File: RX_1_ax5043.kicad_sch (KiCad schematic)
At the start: 18 parts, among them U201 RFShield_OnePiece, U205 AX5043, U206 TPS22919D

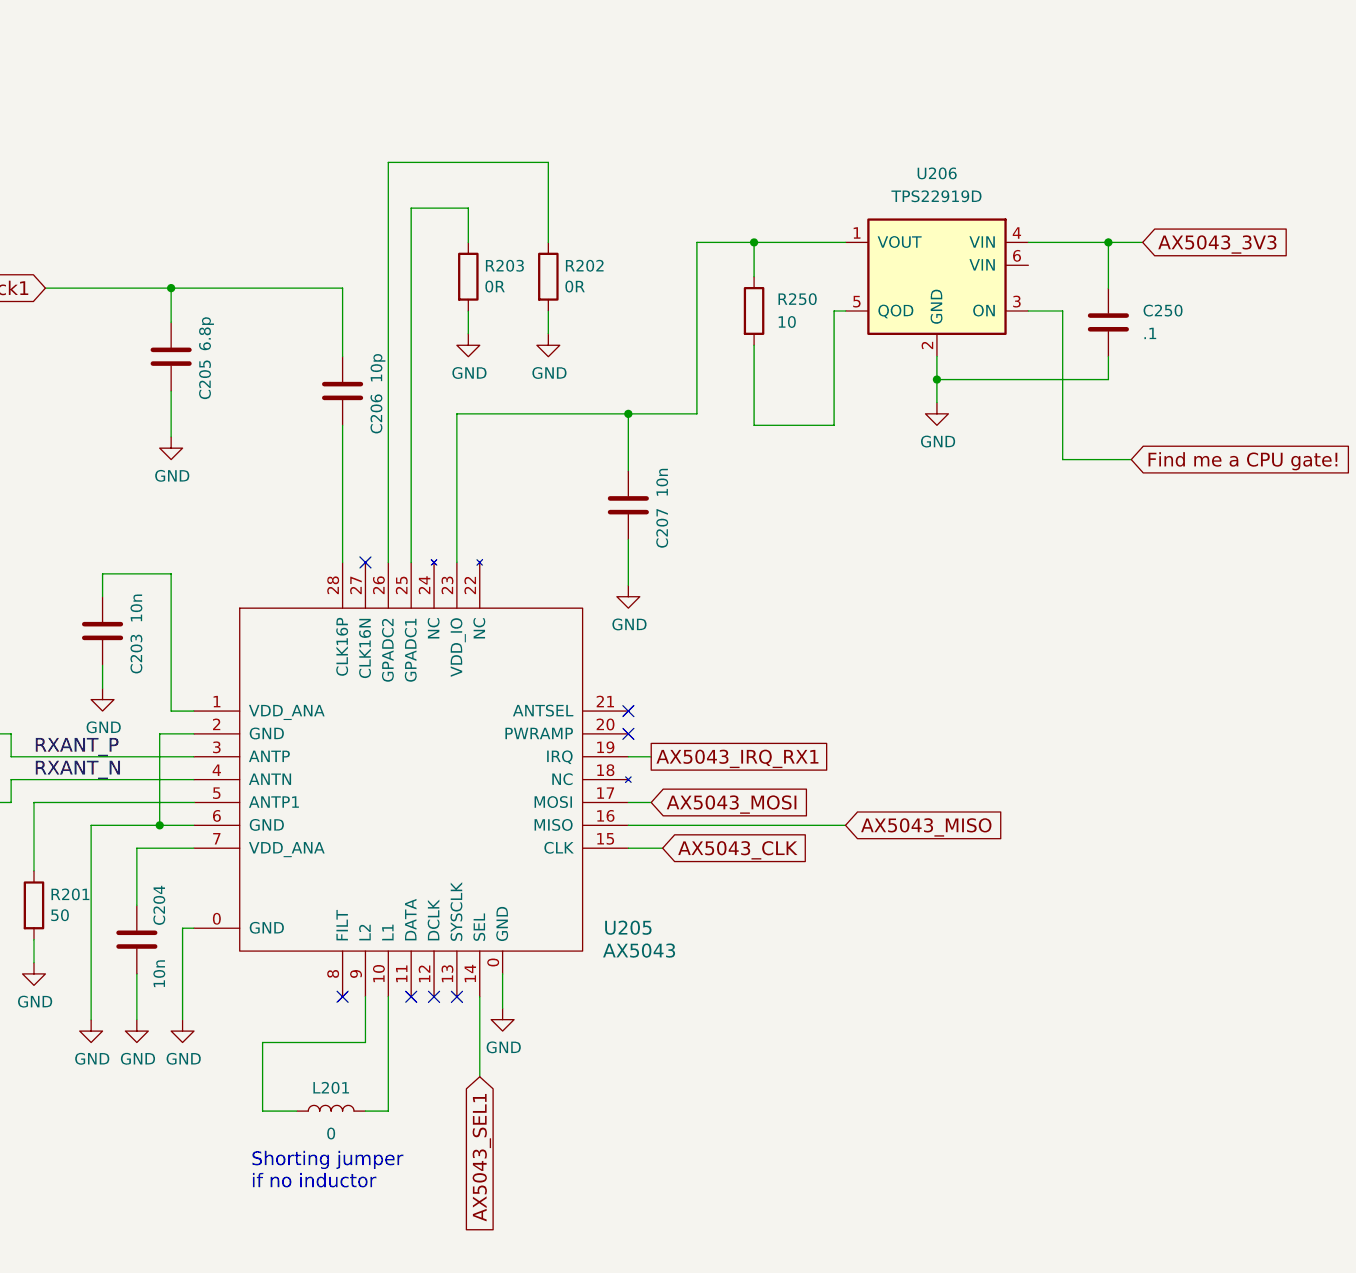
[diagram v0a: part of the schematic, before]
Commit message: Lots of cleanups to fix numerous issues
Signed-off-by: Corey Minyard <corey@minyard.net>
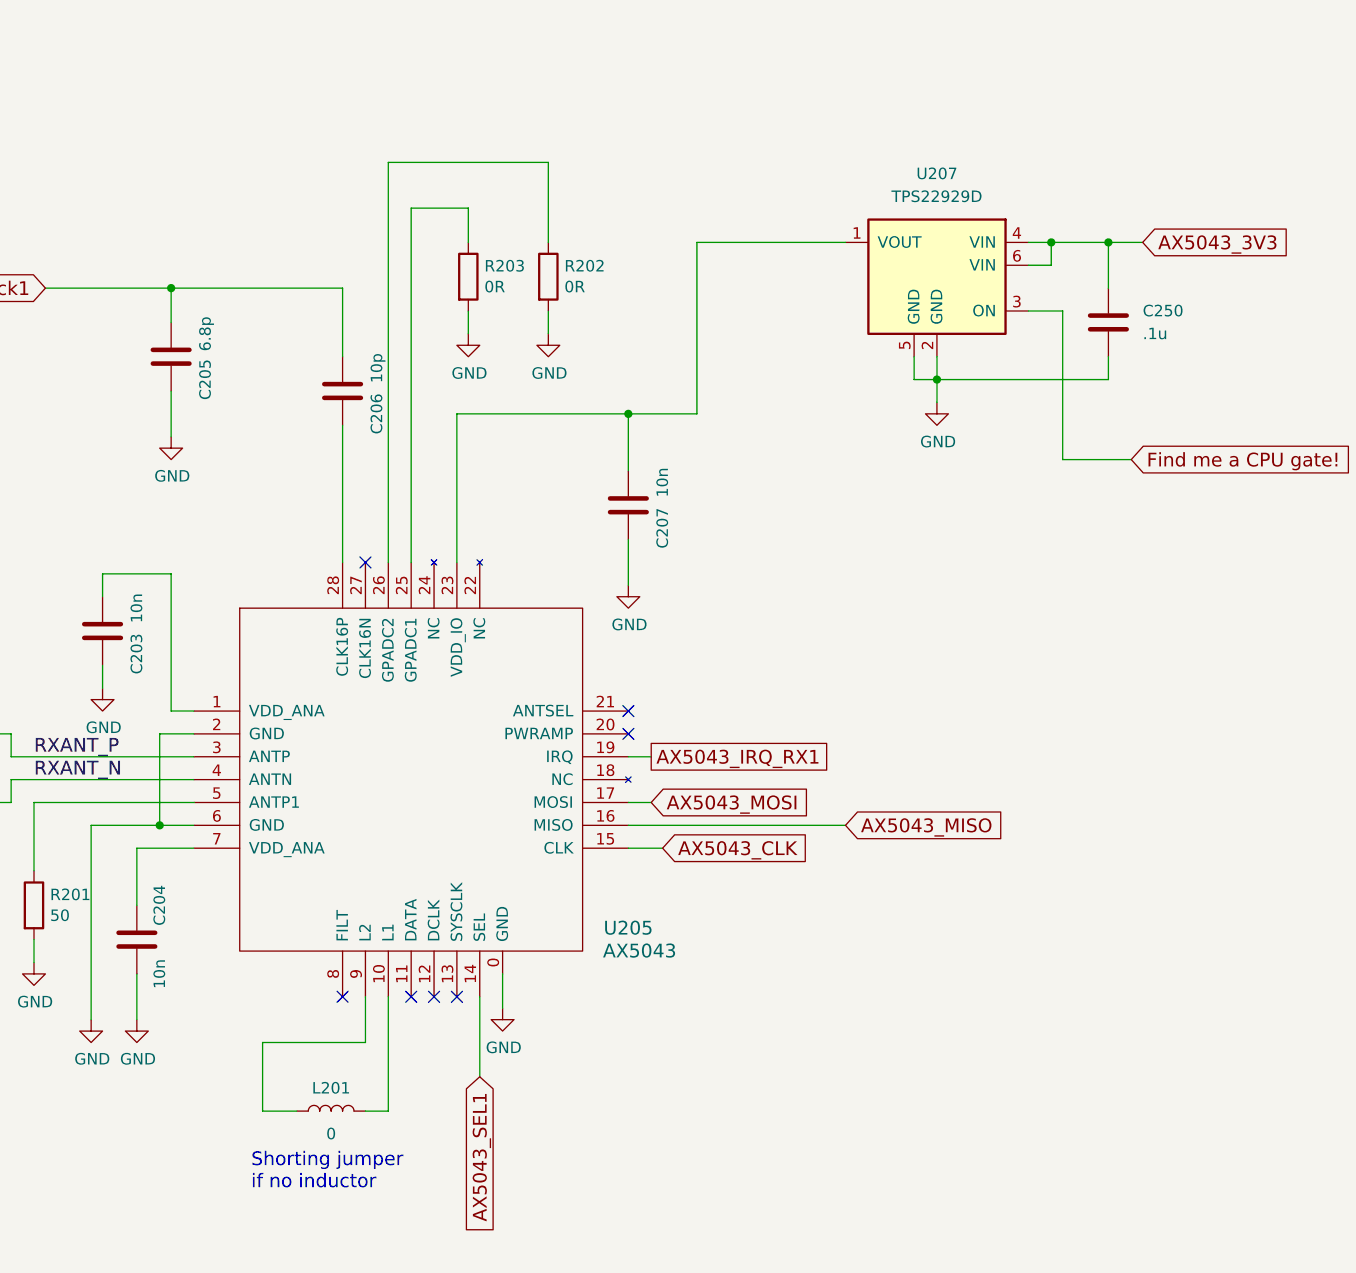
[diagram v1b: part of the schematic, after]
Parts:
- removed R250: 10, symbol Device:R
- C250: value .1 -> .1u; footprint (none) -> Capacitor_SMD:C_0402_1005Metric
- U207: renamed from U206; value TPS22919D -> TPS22929D
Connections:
- net AX5043_3V3: now also U207.6 (VIN)
- net GND: now also U207.5 (GND)

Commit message: Start ripping things apart
Signed-off-by: Corey Minyard <corey@minyard.net>
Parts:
- removed C201, C202: 4p3, Capacitor_SMD:C_0603_1608Metric_Pad1.08x0.95mm_HandSolder, symbol Device:C
- removed P202: ~, PacSatDev_misc:U_FL, symbol PACSAT_DEV_misc:U_FL
- added L90: WBC1-1TL, IND6_WBC1, symbol PACSAT_DEV_misc:WBC1-1TL
- added R89: 10K, Resistor_SMD:R_0603_1608Metric_Pad0.98x0.95mm_HandSolder, symbol Device:R
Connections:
- net GND: now also L90.2, L90.4, R89.2
- net RXANT_N: now also L90.3
- net RXANT_P: now also L90.1
- net Find me a CPU gate! renamed AX5043_EN_RX1
- net AX5043_EN_RX1: now also R89.1
- net RX1_P: no longer names the net of P201.1 (In)
- net RX1_P: now also L90.6
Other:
- note removed: "RX1-"
- note removed: "Short Caps Initially"
- moved on the sheet: P201

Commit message: More hacking on things
Signed-off-by: Corey Minyard <corey@minyard.net>
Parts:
- removed U201: RFShield_OnePiece, PacSatDev_misc:RF_SHIELD_BMI_S_201_F_U201, symbol PACSAT_DEV_misc:RF_SHIELD_BOX

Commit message: Clean up RTC, start working on power
Signed-off-by: Corey Minyard <corey@minyard.net>
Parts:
- L90: footprint IND6_WBC1 -> PacSatDev_misc:IND6_WBC1
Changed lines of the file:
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@@
 			)
 		)
-		(property "Footprint" "IND6_WBC1"
+		(property "Footprint" "PacSatDev_misc:IND6_WBC1"
 			(at 170.18 129.54 0)
 			(effects

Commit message: Finish up most of the ax5043 routing
Signed-off-by: Corey Minyard <corey@minyard.net>
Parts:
- L201: footprint PacSatDev_misc:L_Murata_LQH2MCNxxxx02_2.0x1.6mm -> Inductor_SMD:L_0603_1608Metric_Pad1.05x0.95mm_HandSolder
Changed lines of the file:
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@@
 			)
 		)
-		(property "Footprint" "PacSatDev_misc:L_Murata_LQH2MCNxxxx02_2.0x1.6mm"
+		(property "Footprint" "Inductor_SMD:L_0603_1608Metric_Pad1.05x0.95mm_HandSolder"
 			(at 212.09 172.72 0)
 			(effects

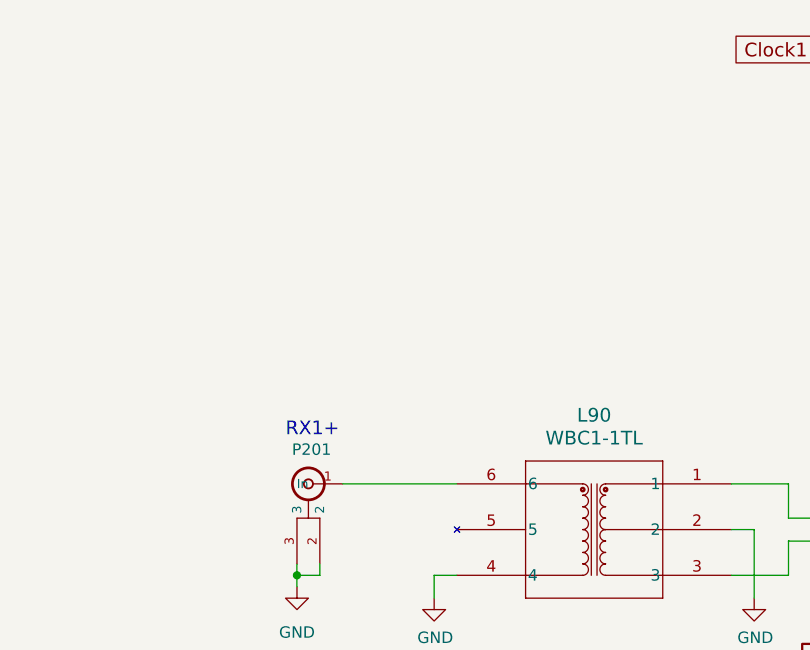
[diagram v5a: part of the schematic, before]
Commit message: Do a lot of routing work
RX input is done, 5043s are done, power is done.

Signed-off-by: Corey Minyard <corey@minyard.net>
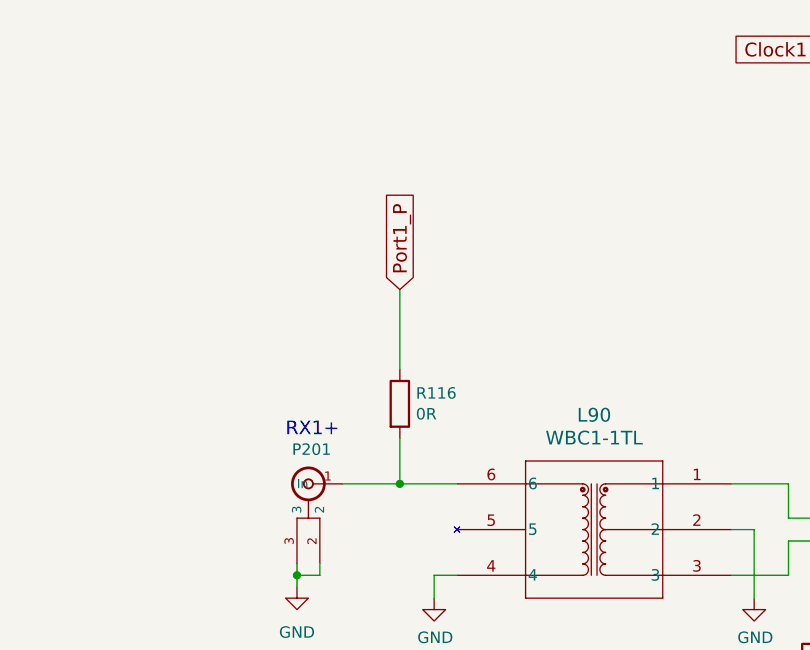
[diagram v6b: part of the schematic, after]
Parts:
- added R116: 0R, Resistor_SMD:R_0603_1608Metric_Pad0.98x0.95mm_HandSolder, symbol Device:R
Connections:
- net at L90.6, P201.1 (In): now also R116.2
- new net Port1_P: R116.1
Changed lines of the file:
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@@
+	)
+	(junction
+		(at 133.35 129.54)
+		(diameter 0)
+		(color 0 0 0 0)
 	)
 	(junction
@@
 	(wire
 		(pts
+			(xy 133.35 129.54) (xy 139.7 129.54)
+		)
+		(stroke
+			(width 0)
+			(type default)
+		)
+	)
+	(wire
+		(pts
 			(xy 279.4 91.44) (xy 298.45 91.44)
 		)
@@
 	(wire
 		(pts
-			(xy 127 129.54) (xy 139.7 129.54)
+			(xy 127 129.54) (xy 133.35 129.54)
 		)
 		(stroke
@@
 	(wire
 		(pts
+			(xy 133.35 124.46) (xy 133.35 129.54)
+		)
+		(stroke
+			(width 0)
+			(type default)
+		)
+	)
+	(wire
+		(pts
 			(xy 245.11 138.43) (xy 247.65 138.43)
 		)
@@
 		(pts
 			(xy 196.85 143.51) (xy 190.5 143.51)
+		)
+		(stroke
+			(width 0)
+			(type default)
+		)
+	)
+	(wire
+		(pts
+			(xy 133.35 107.95) (xy 133.35 116.84)
 		)
 		(stroke
@@
 		(property "Intersheetrefs" "${INTERSHEET_REFS}"
 			(at 265.6275 143.51 0)
+			(effects
+				(font
+					(size 1.27 1.27)
+				)
+				(justify left)
+				(hide yes)
+			)
+		)
+	)
+	(global_label "Port1_P"
+		(shape input)
+		(at 133.35 107.95 90)
+		(fields_autoplaced yes)
+		(effects
+			(font
+				(size 1.524 1.524)
+			)
+			(justify left)
+		)
+		(property "Intersheetrefs" "${INTERSHEET_REFS}"
+			(at 133.35 96.2995 90)
 			(effects
 				(font
@@
 					(unit 1)
 				)
+			)
+		)
+	)
+	(symbol
+		(lib_id "Device:R")
+		(at 133.35 120.65 0)
+		(unit 1)
+		(exclude_from_sim no)
+		(in_bom yes)
+		(on_board yes)
+		(dnp no)
+		(property "Reference" "R116"
+			(at 135.128 119.4816 0)
+			(effects
+				(font
+					(size 1.27 1.27)
+				)
+				(justify left)
+			)
+		)
+		(property "Value" "0R"
+			(at 135.128 121.793 0)
+			(effects
+				(font
+					(size 1.27 1.27)
+				)
+				(justify left)
+			)
+		)
+		(property "Footprint" "Resistor_SMD:R_0603_1608Metric_Pad0.98x0.95mm_HandSolder"
+			(at 131.572 120.65 90)
+			(effects
+				(font
+					(size 1.27 1.27)
+				)
+				(hide yes)
+			)
+		)
+		(property "Datasheet" "~"
+			(at 133.35 120.65 0)
+			(effects
+				(font
+					(size 1.27 1.27)
+				)
+			)
+		)
+		(property "Description" ""
+			(at 133.35 120.65 0)
+			(effects
+				(font
+					(size 1.27 1.27)
+				)
+			)
+		)
+		(pin "1"
+		)
+		(pin "2"
+		)
+		(instances
+			(project "PacSat_AFSK"
+				(path "/cc9f42d2-6985-41ac-acab-5ab7b01c5b38/07d62cf1-e888-4b13-86c4-67d770627579"
+					(reference "R116")
+					(unit 1)
+				)

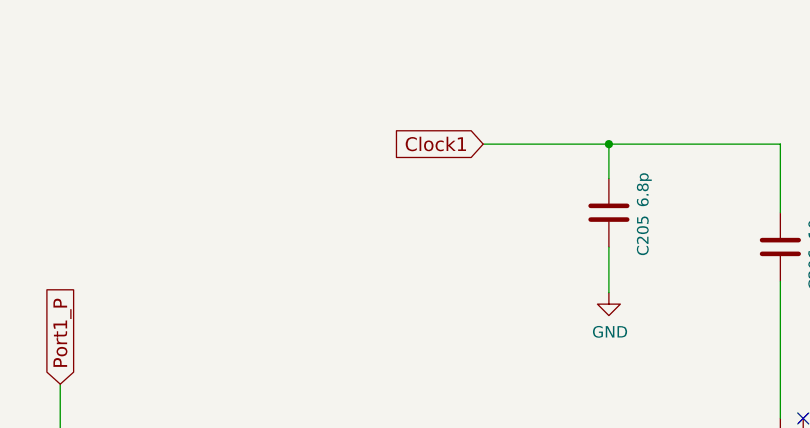
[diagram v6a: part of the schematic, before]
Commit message: Wire in clocks, more cleanups, wire in MRAM
Signed-off-by: Corey Minyard <corey@minyard.net>
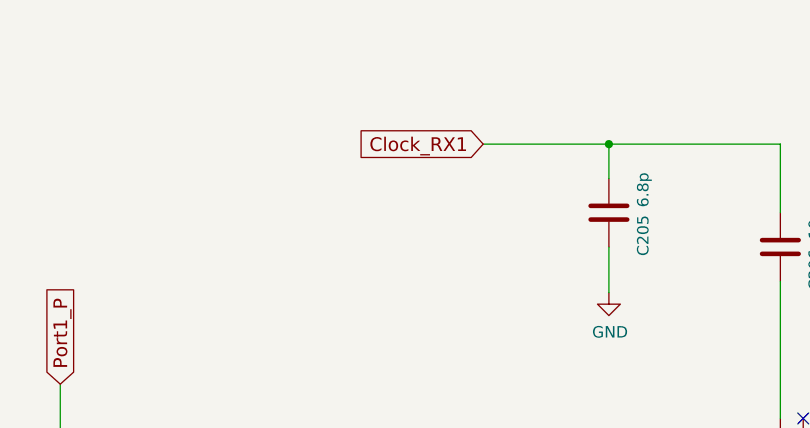
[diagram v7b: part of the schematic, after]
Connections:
- net Clock1 renamed Clock_RX1
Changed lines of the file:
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@@
 		)
 	)
-	(global_label "Clock1"
+	(global_label "Clock_RX1"
 		(shape input)
 		(at 180.34 81.28 180)
@@
 		)
 		(property "Intersheetrefs" "${INTERSHEET_REFS}"
-			(at 169.946 81.28 0)
+			(at 165.7141 81.28 0)
 			(effects
 				(font

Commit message: Add a CPU thermsistor
Signed-off-by: Corey Minyard <corey@minyard.net>
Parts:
- C250: footprint Capacitor_SMD:C_0402_1005Metric -> Capacitor_SMD:C_0603_1608Metric_Pad1.08x0.95mm_HandSolder
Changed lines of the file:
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@@
 			)
 		)
-		(property "Footprint" "Capacitor_SMD:C_0402_1005Metric"
+		(property "Footprint" "Capacitor_SMD:C_0603_1608Metric_Pad1.08x0.95mm_HandSolder"
 			(at 299.4152 88.9 0)
 			(effects
